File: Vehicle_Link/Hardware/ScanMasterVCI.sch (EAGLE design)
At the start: 89 parts, among them IC1 XMEGA32A4U, Q1 MMBT4403, Q10 ZXMP6A17G, Q11 MMBT3904, Q2 MMBT3904, Q3 MMBT3904, Q4 MMBT3904, Q5 MMBT3904, Q6 MMBT3904, Q7 NDC7002N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

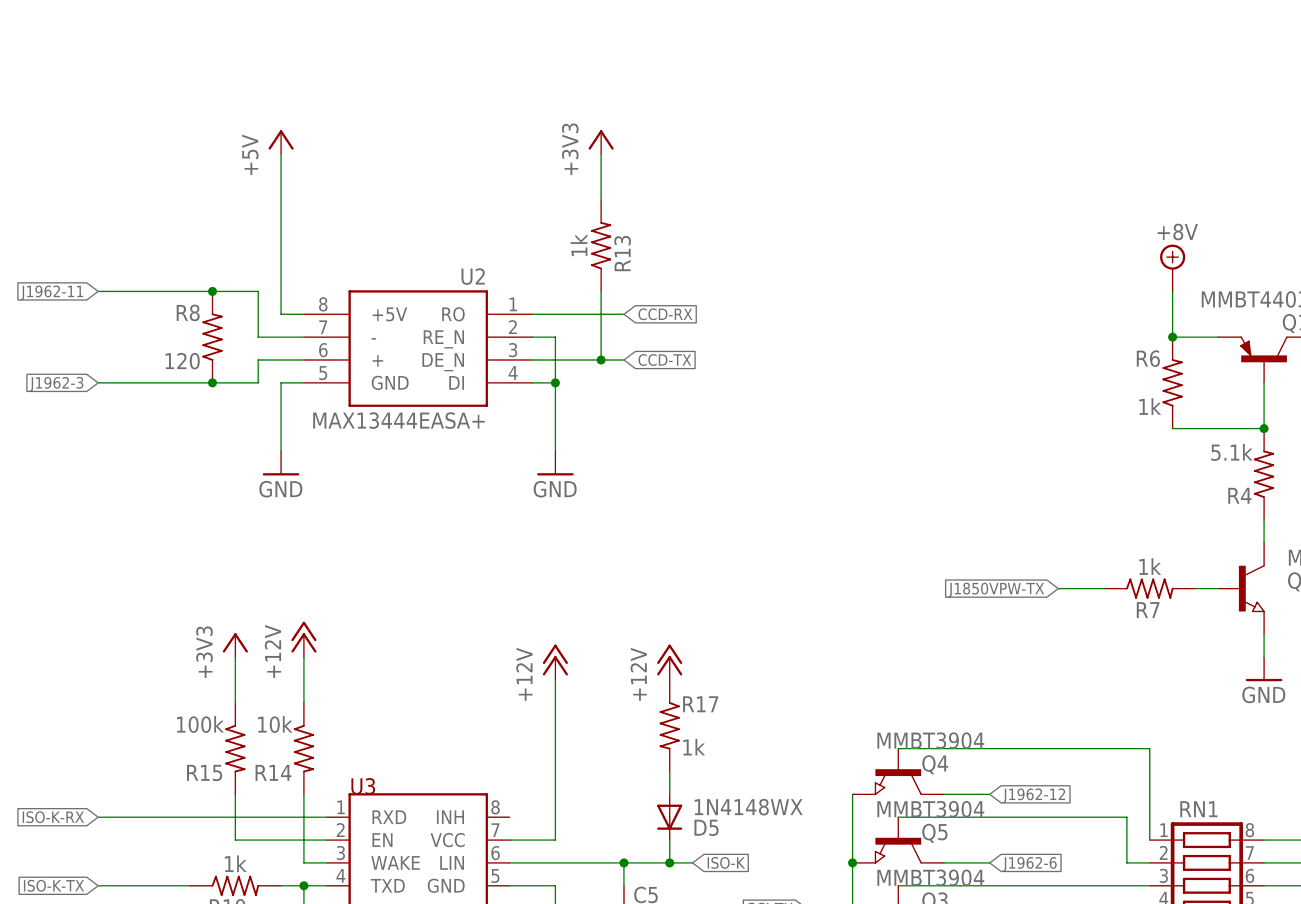
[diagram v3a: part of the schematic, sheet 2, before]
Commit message: Corrected the 8V IC being the wrong way around. Fixed pull-up resistors.
Lots of pull-up resistors were 10k, or even 100k, and that doesn't really seem to work in practical cases, so I've corrected them all to be 1k. For CCD, since I had 3 1K resistors close to each other I've replaced them with a single resistor array.
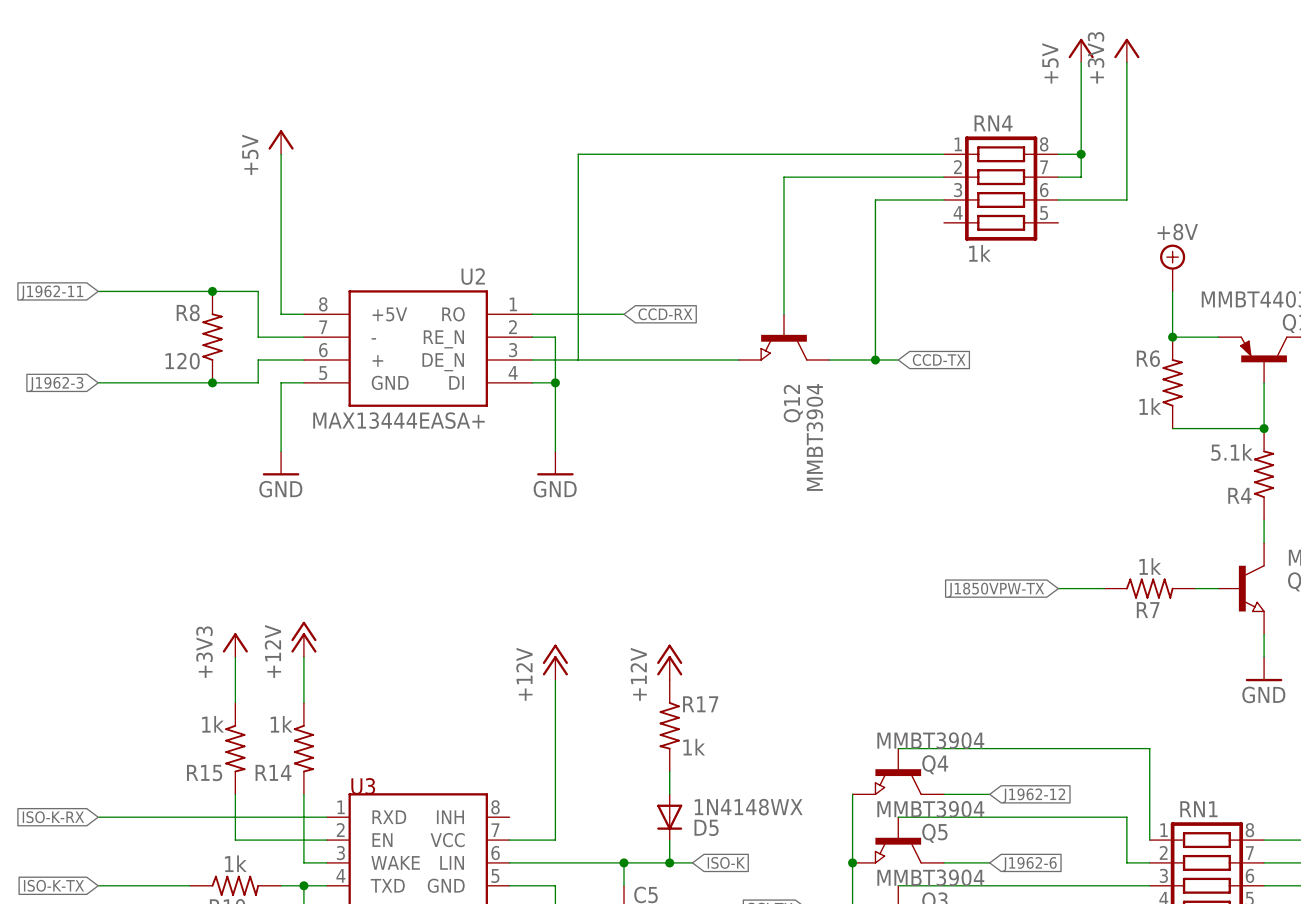
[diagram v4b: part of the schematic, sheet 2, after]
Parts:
- removed R13: 1k, adafruit:R-US_R0603
- added Q12: MMBT3904, semicon-smd-ipc:NPN-TRANSISTOR_SOT23
- added RN4: 1k, resistor-net:CTS742C083
- R14: value 10k -> 1k
- R15: value 100k -> 1k
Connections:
- new net N$32: Q12.E, RN4.1, U2.DE_N
- new net N$33: Q12.B, RN4.2
- net +12V: now also U1.VOUT; no longer U1.VIN
- net +3V3: now also RN4.6; no longer R13.2
- net +5V: now also RN4.7, RN4.8
- net +8V: now also U1.VIN; no longer U1.VOUT
- net CCD-TX: now also Q12.C, RN4.3; no longer R13.1, U2.DE_N
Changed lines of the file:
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@@
 <?xml version="1.0" encoding="utf-8"?>
 <!DOCTYPE eagle SYSTEM "eagle.dtd">
-<eagle version="8.7.0">
+<eagle version="8.4.3">
 <drawing>
 <settings>
@@
 <part name="P+6" library="supply1" library_urn="urn:adsk.eagle:library:371" deviceset="+12V" device=""/>
 <part name="GND1" library="supply1" library_urn="urn:adsk.eagle:library:371" deviceset="GND" device=""/>
-<part name="R14" library="adafruit" library_urn="urn:adsk.eagle:library:420" deviceset="R-US_" device="R0603" value="10k"/>
+<part name="R14" library="adafruit" library_urn="urn:adsk.eagle:library:420" deviceset="R-US_" device="R0603" value="1k"/>
 <part name="P+7" library="supply1" library_urn="urn:adsk.eagle:library:371" deviceset="+12V" device=""/>
 <part name="C5" library="adafruit" library_urn="urn:adsk.eagle:library:420" deviceset="C-US" device="C0603" value="220pF"/>
@@
 <part name="R17" library="adafruit" library_urn="urn:adsk.eagle:library:420" deviceset="R-US_" device="R0603" value="1k"/>
 <part name="GND26" library="supply1" library_urn="urn:adsk.eagle:library:371" deviceset="GND" device=""/>
-<part name="P+4" library="supply1" library_urn="urn:adsk.eagle:library:371" deviceset="+12V" device=""/>
 <part name="SUPPLY1" library="supply2" library_urn="urn:adsk.eagle:library:372" deviceset="+8V" device=""/>
 <part name="R7" library="adafruit" library_urn="urn:adsk.eagle:library:420" deviceset="R-US_" device="R0603" value="1k"/>
@@
 <part name="GND35" library="supply1" library_urn="urn:adsk.eagle:library:371" deviceset="GND" device=""/>
 <part name="P+3" library="supply1" library_urn="urn:adsk.eagle:library:371" deviceset="+12V" device=""/>
-<part name="R15" library="adafruit" library_urn="urn:adsk.eagle:library:420" deviceset="R-US_" device="R0603" value="100k"/>
+<part name="R15" library="adafruit" library_urn="urn:adsk.eagle:library:420" deviceset="R-US_" device="R0603" value="1k"/>
 <part name="+3V5" library="supply1" library_urn="urn:adsk.eagle:library:371" deviceset="+3V3" device=""/>
 <part name="R16" library="adafruit" library_urn="urn:adsk.eagle:library:420" deviceset="R-US_" device="R0603" value="1k"/>
@@
 <part name="GND3" library="supply1" library_urn="urn:adsk.eagle:library:371" deviceset="GND" device=""/>
 <part name="GND4" library="supply1" library_urn="urn:adsk.eagle:library:371" deviceset="GND" device=""/>
-<part name="R13" library="adafruit" library_urn="urn:adsk.eagle:library:420" deviceset="R-US_" device="R0603" value="1k"/>
-<part name="+3V3" library="supply1" library_urn="urn:adsk.eagle:library:371" deviceset="+3V3" device=""/>
+<part name="P+4" library="supply1" library_urn="urn:adsk.eagle:library:371" deviceset="+12V" device=""/>
+<part name="Q12" library="semicon-smd-ipc" library_urn="urn:adsk.eagle:library:353" deviceset="NPN-TRANSISTOR_" device="SOT23" package3d_urn="urn:adsk.eagle:package:26310/1" value="MMBT3904"/>
+<part name="P+13" library="supply1" library_urn="urn:adsk.eagle:library:371" deviceset="+5V" device=""/>
+<part name="RN4" library="resistor-net" library_urn="urn:adsk.eagle:library:343" deviceset="CTS742C083" device="" package3d_urn="urn:adsk.eagle:package:24985/1" value="1k"/>
+<part name="+3V11" library="supply1" library_urn="urn:adsk.eagle:library:371" deviceset="+3V3" device=""/>
 </parts>
 <sheets>
@@
 <instance part="GND19" gate="1" x="187.96" y="91.44"/>
 <instance part="GND26" gate="1" x="63.5" y="101.6"/>
-<instance part="P+4" gate="1" x="63.5" y="119.38"/>
-<instance part="SUPPLY1" gate="+8V" x="88.9" y="116.84"/>
+<instance part="SUPPLY1" gate="+8V" x="63.5" y="119.38"/>
 <instance part="U1" gate="G$1" x="76.2" y="109.22"/>
 <instance part="U4" gate="G$1" x="170.18" y="71.12"/>
@@
 <instance part="LED2" gate="G$1" x="119.38" y="12.7" rot="R270"/>
 <instance part="GND25" gate="1" x="111.76" y="5.08"/>
+<instance part="P+4" gate="1" x="88.9" y="121.92"/>
 </instances>
 <busses>
@@
 </segment>
 <segment>
-<wire x1="66.04" y1="111.76" x2="63.5" y2="111.76" width="0.1524" layer="91"/>
-<wire x1="63.5" y1="111.76" x2="63.5" y2="116.84" width="0.1524" layer="91"/>
+<pinref part="U1" gate="G$1" pin="VOUT"/>
+<wire x1="86.36" y1="109.22" x2="88.9" y2="109.22" width="0.1524" layer="91"/>
+<wire x1="88.9" y1="109.22" x2="88.9" y2="119.38" width="0.1524" layer="91"/>
 <pinref part="P+4" gate="1" pin="+12V"/>
-<pinref part="U1" gate="G$1" pin="VIN"/>
 </segment>
 </net>
@@
 <net name="+8V" class="2">
 <segment>
-<wire x1="86.36" y1="109.22" x2="88.9" y2="109.22" width="0.1524" layer="91"/>
-<wire x1="88.9" y1="109.22" x2="88.9" y2="114.3" width="0.1524" layer="91"/>
+<wire x1="63.5" y1="111.76" x2="63.5" y2="116.84" width="0.1524" layer="91"/>
 <pinref part="SUPPLY1" gate="+8V" pin="+8V"/>
-<pinref part="U1" gate="G$1" pin="VOUT"/>
+<pinref part="U1" gate="G$1" pin="VIN"/>
+<wire x1="63.5" y1="111.76" x2="66.04" y2="111.76" width="0.1524" layer="91"/>
 </segment>
 </net>
@@
 <instance part="GND3" gate="1" x="60.96" y="182.88"/>
 <instance part="GND4" gate="1" x="30.48" y="182.88"/>
-<instance part="R13" gate="G$1" x="66.04" y="208.28" smashed="yes" rot="R90">
-<attribute name="NAME" x="67.5386" y="209.55" size="1.778" layer="95" rot="R270"/>
-<attribute name="VALUE" x="62.738" y="209.55" size="1.778" layer="96" rot="R270"/>
-</instance>
-<instance part="+3V3" gate="G$1" x="66.04" y="220.98"/>
+<instance part="Q12" gate="G$1" x="86.36" y="198.12" smashed="yes" rot="R270">
+<attribute name="NAME" x="86.36" y="193.04" size="1.778" layer="95" rot="R270"/>
+<attribute name="VALUE" x="88.9" y="193.04" size="1.778" layer="96" rot="R270"/>
+</instance>
+<instance part="P+13" gate="1" x="119.38" y="231.14"/>
+<instance part="RN4" gate="G$1" x="109.22" y="215.9"/>
+<instance part="+3V11" gate="G$1" x="124.46" y="231.14"/>
 </instances>
 <busses>
@@
 </segment>
 <segment>
-<pinref part="R13" gate="G$1" pin="2"/>
-<pinref part="+3V3" gate="G$1" pin="+3V3"/>
-<wire x1="66.04" y1="213.36" x2="66.04" y2="218.44" width="0.1524" layer="91"/>
+<pinref part="RN4" gate="G$1" pin="6"/>
+<wire x1="116.84" y1="213.36" x2="124.46" y2="213.36" width="0.1524" layer="91"/>
+<wire x1="124.46" y1="213.36" x2="124.46" y2="228.6" width="0.1524" layer="91"/>
+<pinref part="+3V11" gate="G$1" pin="+3V3"/>
 </segment>
 </net>
@@
 <junction x="190.5" y="162.56"/>
 </segment>
+<segment>
+<pinref part="P+13" gate="1" pin="+5V"/>
+<wire x1="119.38" y1="215.9" x2="119.38" y2="218.44" width="0.1524" layer="91"/>
+<pinref part="RN4" gate="G$1" pin="7"/>
+<wire x1="119.38" y1="218.44" x2="119.38" y2="228.6" width="0.1524" layer="91"/>
+<wire x1="119.38" y1="215.9" x2="116.84" y2="215.9" width="0.1524" layer="91"/>
+<pinref part="RN4" gate="G$1" pin="8"/>
+<wire x1="116.84" y1="218.44" x2="119.38" y2="218.44" width="0.1524" layer="91"/>
+<junction x="119.38" y="218.44"/>
+</segment>
 </net>
 <net name="J1850VPW-TX" class="0">
@@
 <net name="CCD-TX" class="0">
 <segment>
-<label x="68.58" y="195.58" size="1.27" layer="95" xref="yes"/>
-<pinref part="U2" gate="G$1" pin="DE_N"/>
-<wire x1="68.58" y1="195.58" x2="66.04" y2="195.58" width="0.1524" layer="91"/>
-<pinref part="R13" gate="G$1" pin="1"/>
-<wire x1="66.04" y1="195.58" x2="58.42" y2="195.58" width="0.1524" layer="91"/>
-<wire x1="66.04" y1="195.58" x2="66.04" y2="203.2" width="0.1524" layer="91"/>
-<junction x="66.04" y="195.58"/>
+<label x="99.06" y="195.58" size="1.27" layer="95" xref="yes"/>
+<pinref part="Q12" gate="G$1" pin="C"/>
+<wire x1="91.44" y1="195.58" x2="96.52" y2="195.58" width="0.1524" layer="91"/>
+<wire x1="96.52" y1="195.58" x2="99.06" y2="195.58" width="0.1524" layer="91"/>
+<junction x="96.52" y="195.58"/>
+<pinref part="RN4" gate="G$1" pin="3"/>
+<wire x1="96.52" y1="195.58" x2="96.52" y2="213.36" width="0.1524" layer="91"/>
+<wire x1="96.52" y1="213.36" x2="104.14" y2="213.36" width="0.1524" layer="91"/>
 </segment>
 </net>
@@
 </segment>
 </net>
+<net name="N$32" class="0">
+<segment>
+<pinref part="Q12" gate="G$1" pin="E"/>
+<pinref part="U2" gate="G$1" pin="DE_N"/>
+<wire x1="81.28" y1="195.58" x2="63.5" y2="195.58" width="0.1524" layer="91"/>
+<wire x1="63.5" y1="195.58" x2="58.42" y2="195.58" width="0.1524" layer="91"/>
+<wire x1="63.5" y1="195.58" x2="63.5" y2="218.44" width="0.1524" layer="91"/>
+<pinref part="RN4" gate="G$1" pin="1"/>
+<wire x1="63.5" y1="218.44" x2="104.14" y2="218.44" width="0.1524" layer="91"/>
+</segment>
+</net>
+<net name="N$33" class="0">
+<segment>
+<pinref part="Q12" gate="G$1" pin="B"/>
+<pinref part="RN4" gate="G$1" pin="2"/>
+<wire x1="104.14" y1="215.9" x2="86.36" y2="215.9" width="0.1524" layer="91"/>
+<wire x1="86.36" y1="215.9" x2="86.36" y2="200.66" width="0.1524" layer="91"/>
+</segment>
+</net>

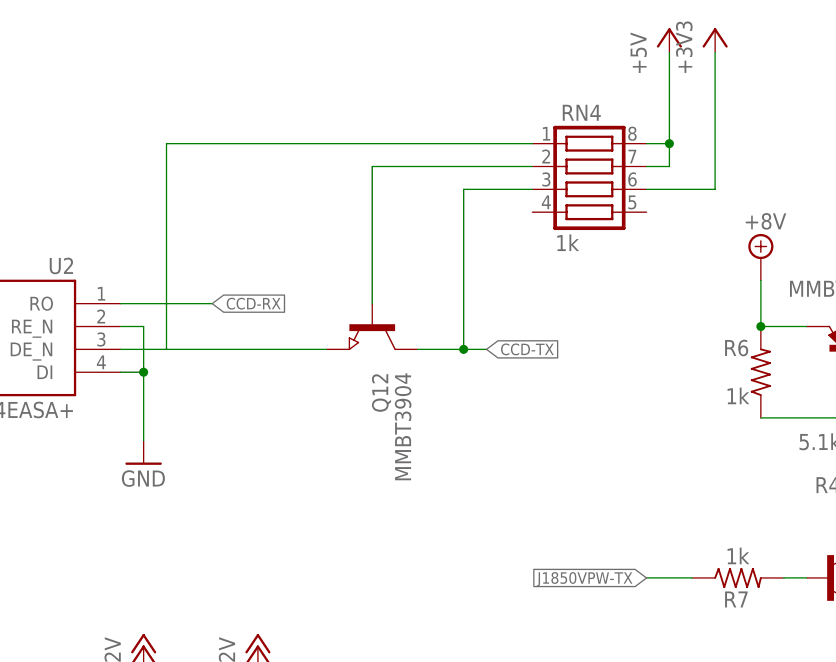
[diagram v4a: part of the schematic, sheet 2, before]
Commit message: Made some landing pad changes to the voltage IC's, to fix heat issues I saw. Started looking into simplifying the circuit to get rid of some of the vias.
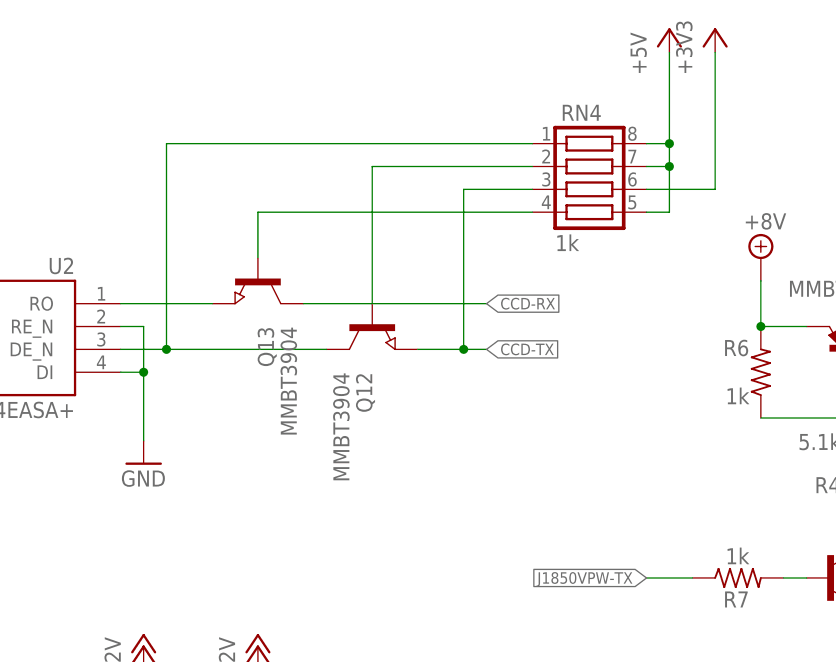
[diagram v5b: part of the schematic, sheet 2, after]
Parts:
- added Q13: MMBT3904, semicon-smd-ipc:NPN-TRANSISTOR_SOT23
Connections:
- new net N$34: Q13.E, U2.RO
- new net N$35: Q13.B, RN4.4
- net +5V: now also RN4.5
- net CCD-RX: now also Q13.C; no longer U2.RO
- net CCD-TX: now also Q12.E; no longer Q12.C
- net N$32: now also Q12.C; no longer Q12.E
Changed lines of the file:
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@@
 <part name="RN4" library="resistor-net" library_urn="urn:adsk.eagle:library:343" deviceset="CTS742C083" device="" package3d_urn="urn:adsk.eagle:package:24985/1" value="1k"/>
 <part name="+3V11" library="supply1" library_urn="urn:adsk.eagle:library:371" deviceset="+3V3" device=""/>
+<part name="Q13" library="semicon-smd-ipc" library_urn="urn:adsk.eagle:library:353" deviceset="NPN-TRANSISTOR_" device="SOT23" package3d_urn="urn:adsk.eagle:package:26310/1" value="MMBT3904"/>
 </parts>
 <sheets>
@@
 <instance part="GND3" gate="1" x="60.96" y="182.88"/>
 <instance part="GND4" gate="1" x="30.48" y="182.88"/>
-<instance part="Q12" gate="G$1" x="86.36" y="198.12" smashed="yes" rot="R270">
-<attribute name="NAME" x="86.36" y="193.04" size="1.778" layer="95" rot="R270"/>
-<attribute name="VALUE" x="88.9" y="193.04" size="1.778" layer="96" rot="R270"/>
+<instance part="Q12" gate="G$1" x="86.36" y="198.12" smashed="yes" rot="MR270">
+<attribute name="NAME" x="86.36" y="193.04" size="1.778" layer="95" rot="MR270"/>
+<attribute name="VALUE" x="83.82" y="193.04" size="1.778" layer="96" rot="MR270"/>
 </instance>
 <instance part="P+13" gate="1" x="119.38" y="231.14"/>
 <instance part="RN4" gate="G$1" x="109.22" y="215.9"/>
 <instance part="+3V11" gate="G$1" x="124.46" y="231.14"/>
+<instance part="Q13" gate="G$1" x="73.66" y="203.2" smashed="yes" rot="R270">
+<attribute name="NAME" x="73.66" y="198.12" size="1.778" layer="95" rot="R270"/>
+<attribute name="VALUE" x="76.2" y="198.12" size="1.778" layer="96" rot="R270"/>
+</instance>
 </instances>
 <busses>
@@
 <wire x1="116.84" y1="218.44" x2="119.38" y2="218.44" width="0.1524" layer="91"/>
 <junction x="119.38" y="218.44"/>
+<pinref part="RN4" gate="G$1" pin="5"/>
+<wire x1="116.84" y1="210.82" x2="119.38" y2="210.82" width="0.1524" layer="91"/>
+<wire x1="119.38" y1="210.82" x2="119.38" y2="215.9" width="0.1524" layer="91"/>
+<junction x="119.38" y="215.9"/>
 </segment>
 </net>
@@
 <segment>
 <label x="99.06" y="195.58" size="1.27" layer="95" xref="yes"/>
-<pinref part="Q12" gate="G$1" pin="C"/>
-<wire x1="91.44" y1="195.58" x2="96.52" y2="195.58" width="0.1524" layer="91"/>
 <wire x1="96.52" y1="195.58" x2="99.06" y2="195.58" width="0.1524" layer="91"/>
-<junction x="96.52" y="195.58"/>
 <pinref part="RN4" gate="G$1" pin="3"/>
 <wire x1="96.52" y1="195.58" x2="96.52" y2="213.36" width="0.1524" layer="91"/>
 <wire x1="96.52" y1="213.36" x2="104.14" y2="213.36" width="0.1524" layer="91"/>
+<pinref part="Q12" gate="G$1" pin="E"/>
+<wire x1="91.44" y1="195.58" x2="96.52" y2="195.58" width="0.1524" layer="91"/>
+<junction x="96.52" y="195.58"/>
 </segment>
 </net>
 <net name="CCD-RX" class="0">
 <segment>
-<label x="68.58" y="200.66" size="1.27" layer="95" xref="yes"/>
-<pinref part="U2" gate="G$1" pin="RO"/>
-<wire x1="68.58" y1="200.66" x2="58.42" y2="200.66" width="0.1524" layer="91"/>
+<label x="99.06" y="200.66" size="1.27" layer="95" xref="yes"/>
+<pinref part="Q13" gate="G$1" pin="C"/>
+<wire x1="78.74" y1="200.66" x2="99.06" y2="200.66" width="0.1524" layer="91"/>
 </segment>
 </net>
@@
 <net name="N$32" class="0">
 <segment>
-<pinref part="Q12" gate="G$1" pin="E"/>
 <pinref part="U2" gate="G$1" pin="DE_N"/>
-<wire x1="81.28" y1="195.58" x2="63.5" y2="195.58" width="0.1524" layer="91"/>
 <wire x1="63.5" y1="195.58" x2="58.42" y2="195.58" width="0.1524" layer="91"/>
 <wire x1="63.5" y1="195.58" x2="63.5" y2="218.44" width="0.1524" layer="91"/>
 <pinref part="RN4" gate="G$1" pin="1"/>
 <wire x1="63.5" y1="218.44" x2="104.14" y2="218.44" width="0.1524" layer="91"/>
+<pinref part="Q12" gate="G$1" pin="C"/>
+<wire x1="81.28" y1="195.58" x2="63.5" y2="195.58" width="0.1524" layer="91"/>
+<junction x="63.5" y="195.58"/>
 </segment>
 </net>
@@
 </segment>
 </net>
+<net name="N$34" class="0">
+<segment>
+<pinref part="Q13" gate="G$1" pin="E"/>
+<pinref part="U2" gate="G$1" pin="RO"/>
+<wire x1="68.58" y1="200.66" x2="58.42" y2="200.66" width="0.1524" layer="91"/>
+</segment>
+</net>
+<net name="N$35" class="0">
+<segment>
+<pinref part="Q13" gate="G$1" pin="B"/>
+<pinref part="RN4" gate="G$1" pin="4"/>
+<wire x1="73.66" y1="205.74" x2="73.66" y2="210.82" width="0.1524" layer="91"/>
+<wire x1="73.66" y1="210.82" x2="104.14" y2="210.82" width="0.1524" layer="91"/>
+</segment>
+</net>
